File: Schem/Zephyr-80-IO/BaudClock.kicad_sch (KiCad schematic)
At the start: 3 parts, among them U3 SN74HC4040DR, Y1 ECS-2100AX-147.4

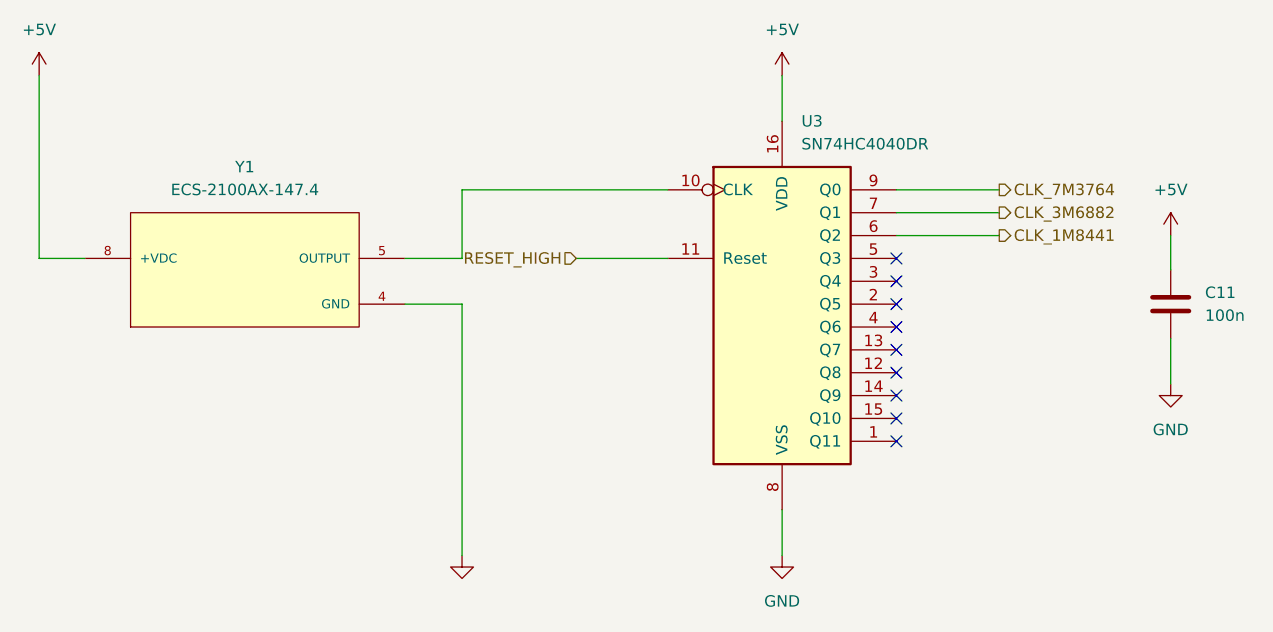
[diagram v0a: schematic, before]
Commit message: Completed the IO Controller schematic and PCB layout for the Zephyr-80 project. This includes the design of the Baud Clock, CPU Address Decoding, Console Port, Device Select Decode, GPIO User Serial, and the main IO Controller schematics. Additionally, the PCB layout for the Zephyr-80 IO board has been created, along with the necessary library files and documentation for the control signal mapping.
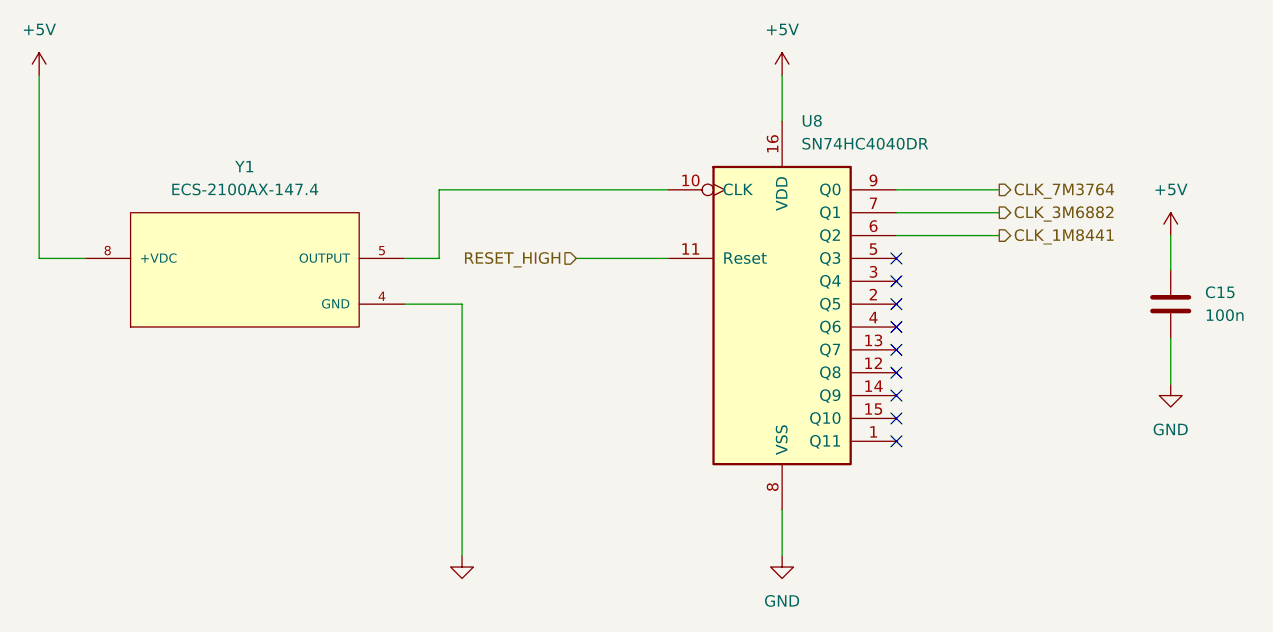
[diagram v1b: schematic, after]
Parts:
- U8: renamed from U3; footprint Package_SO:SO-16_3.9x9.9mm_P1.27mm -> Package_SO:TSSOP-16_4.4x5mm_P0.65mm; MANUFACTURER_PART_NUMBER SN74HC4040DR -> MC74HC4040ADTR2G
- renumbered C11 to C15
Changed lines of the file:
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@@
 	(wire
 		(pts
-			(xy 92.71 69.85) (xy 99.06 69.85)
+			(xy 92.71 69.85) (xy 96.52 69.85)
 		)
 		(stroke
@@
 	(wire
 		(pts
-			(xy 99.06 69.85) (xy 99.06 62.23)
+			(xy 96.52 69.85) (xy 96.52 62.23)
 		)
 		(stroke
@@
 	(wire
 		(pts
-			(xy 99.06 62.23) (xy 121.92 62.23)
+			(xy 96.52 62.23) (xy 121.92 62.23)
 		)
 		(stroke
@@
 		(dnp no)
 		(fields_autoplaced yes)
-		(property "Reference" "#PWR035"
+		(property "Reference" "#PWR045"
 			(at 99.06 109.22 0)
 			(effects
@@
 			(project "Zephyr-80-IO"
 				(path "/db33a8e4-587d-4e74-8d3f-b68910957121/1e002eec-a925-41bd-9968-565c74f66dea"
-					(reference "#PWR035")
+					(reference "#PWR045")
 					(unit 1)
 				)
@@
 		(dnp no)
 		(fields_autoplaced yes)
-		(property "Reference" "#PWR032"
+		(property "Reference" "#PWR042"
 			(at 134.62 53.34 0)
 			(effects
@@
 			(project "Zephyr-80-IO"
 				(path "/db33a8e4-587d-4e74-8d3f-b68910957121/1e002eec-a925-41bd-9968-565c74f66dea"
-					(reference "#PWR032")
+					(reference "#PWR042")
 					(unit 1)
 				)
@@
 		(dnp no)
 		(fields_autoplaced yes)
-		(property "Reference" "#PWR034"
+		(property "Reference" "#PWR044"
 			(at 177.8 90.17 0)
 			(effects
@@
 			(project "Zephyr-80-IO"
 				(path "/db33a8e4-587d-4e74-8d3f-b68910957121/1e002eec-a925-41bd-9968-565c74f66dea"
-					(reference "#PWR034")
+					(reference "#PWR044")
 					(unit 1)
 				)
@@
 		(dnp no)
 		(fields_autoplaced yes)
-		(property "Reference" "C11"
+		(property "Reference" "C15"
 			(at 181.61 73.6599 0)
 			(effects
@@
 			(project "Zephyr-80-IO"
 				(path "/db33a8e4-587d-4e74-8d3f-b68910957121/1e002eec-a925-41bd-9968-565c74f66dea"
-					(reference "C11")
+					(reference "C15")
 					(unit 1)
 				)
@@
 		(dnp no)
 		(fields_autoplaced yes)
-		(property "Reference" "#PWR033"
+		(property "Reference" "#PWR043"
 			(at 177.8 71.12 0)
 			(effects
@@
 			(project "Zephyr-80-IO"
 				(path "/db33a8e4-587d-4e74-8d3f-b68910957121/1e002eec-a925-41bd-9968-565c74f66dea"
-					(reference "#PWR033")
+					(reference "#PWR043")
 					(unit 1)
 				)
@@
 		(dnp no)
 		(fields_autoplaced yes)
-		(property "Reference" "#PWR031"
+		(property "Reference" "#PWR041"
 			(at 52.07 53.34 0)
 			(effects
@@
 			(project "Zephyr-80-IO"
 				(path "/db33a8e4-587d-4e74-8d3f-b68910957121/1e002eec-a925-41bd-9968-565c74f66dea"
-					(reference "#PWR031")
+					(reference "#PWR041")
 					(unit 1)
 				)
@@
 		(dnp no)
 		(fields_autoplaced yes)
-		(property "Reference" "U3"
+		(property "Reference" "U8"
 			(at 136.7633 54.61 0)
 			(effects
@@
 			)
 		)
-		(property "Footprint" "Package_SO:SO-16_3.9x9.9mm_P1.27mm"
+		(property "Footprint" "Package_SO:TSSOP-16_4.4x5mm_P0.65mm"
 			(at 134.62 74.93 0)
 			(effects
@@
 			)
 		)
-		(property "MANUFACTURER_PART_NUMBER" "SN74HC4040DR"
+		(property "MANUFACTURER_PART_NUMBER" "MC74HC4040ADTR2G"
 			(at 134.62 74.93 0)
 			(effects
@@
 			(project "Zephyr-80-IO"
 				(path "/db33a8e4-587d-4e74-8d3f-b68910957121/1e002eec-a925-41bd-9968-565c74f66dea"
-					(reference "U3")
+					(reference "U8")
 					(unit 1)
 				)
@@
 		(dnp no)
 		(fields_autoplaced yes)
-		(property "Reference" "#PWR036"
+		(property "Reference" "#PWR046"
 			(at 134.62 109.22 0)
 			(effects
@@
 			(project "Zephyr-80-IO"
 				(path "/db33a8e4-587d-4e74-8d3f-b68910957121/1e002eec-a925-41bd-9968-565c74f66dea"
-					(reference "#PWR036")
+					(reference "#PWR046")
 					(unit 1)
 				)

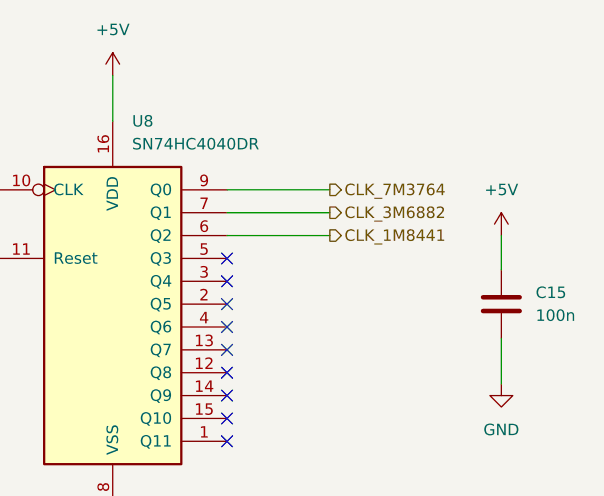
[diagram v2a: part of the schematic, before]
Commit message: Fixed a few mistakes in the IO Controller
* Wrong layer for vertical traces (should not be on the same layer as vcc plane)
* Added pull-downs for DCD for all SIOs (we don't use this line)
* Connected DCD and CTS to the MCU for SIO1 in case we want to use it to gate the SIO1
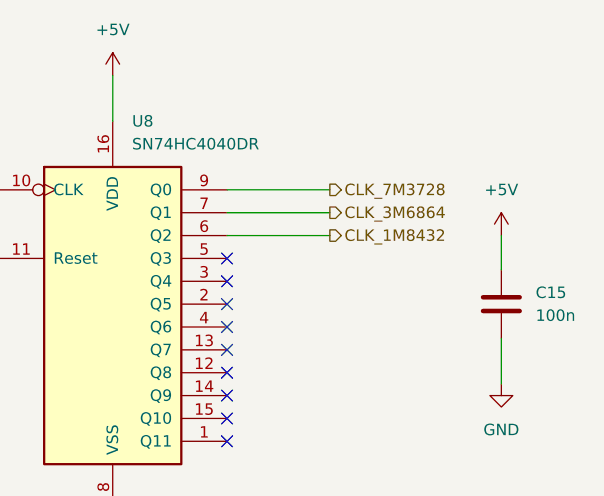
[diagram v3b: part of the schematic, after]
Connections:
- net CLK_1M8441 renamed CLK_1M8432
- net CLK_3M6882 renamed CLK_3M6864
- net CLK_7M3764 renamed CLK_7M3728
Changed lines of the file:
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@@
 		)
 	)
-	(hierarchical_label "CLK_1M8441"
+	(hierarchical_label "CLK_1M8432"
 		(shape output)
 		(at 158.75 67.31 0)
@@
 		)
 	)
-	(hierarchical_label "CLK_7M3764"
+	(hierarchical_label "CLK_7M3728"
 		(shape output)
 		(at 158.75 62.23 0)
@@
 		)
 	)
-	(hierarchical_label "CLK_3M6882"
+	(hierarchical_label "CLK_3M6864"
 		(shape output)
 		(at 158.75 64.77 0)
